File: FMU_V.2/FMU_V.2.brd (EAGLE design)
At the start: 90.2 x 95.9 mm, 322 parts, among them J201 HEADER_1X4, J202 HEADER_1X4, J203 HEADER_1X4, J204 HEADER_1X4, J301 HEADER_1X4, J302 HEADER_1X4, J303 HEADER_1X4, J401 HEADER_1X4, J402 HEADER_1X4, J403 HEADER_1X4, J404 HEADER_1X4, J701 HEADER_1X4, J901 HEADER_1X4, J902 HEADER_1X4, M3_MOUNT1 MOUNT-HOLE3.1MM, M3_MOUNT2 MOUNT-HOLE3.1MM, M3_MOUNT3 MOUNT-HOLE3.1MM, M3_MOUNT4 MOUNT-HOLE3.1MM, U101 STM32F4X7VX, U102 FM25V01, U201 TXS0108TSSOP-20, U202 LT3469, U301 2908-05WB-MG, U302 NUF2042XV6, U303 ADUM5402, U304 MAX13487E, U305 MAX232ECWE, U401 ADUM5402, U402 MAX3051, U403 MAX3051, U502 ICM20608-G, U503 MPU-9250, U504 MPU-6000, U506 MS5611-01BA, U601 BQ24315, U602 BQ24315, U603 LD1117ASTR, U604 LD1117ASTR, U701 STM32F10XCXT6, U801 TXS0108TSSOP-20, U803 LD1117ASTR, U901 LM5005, U902 LM5005, X101 NX3225SA-24.000MHZ-STD-CSR-1, X701 NX3225SA-24.000MHZ-STD-CSR-1

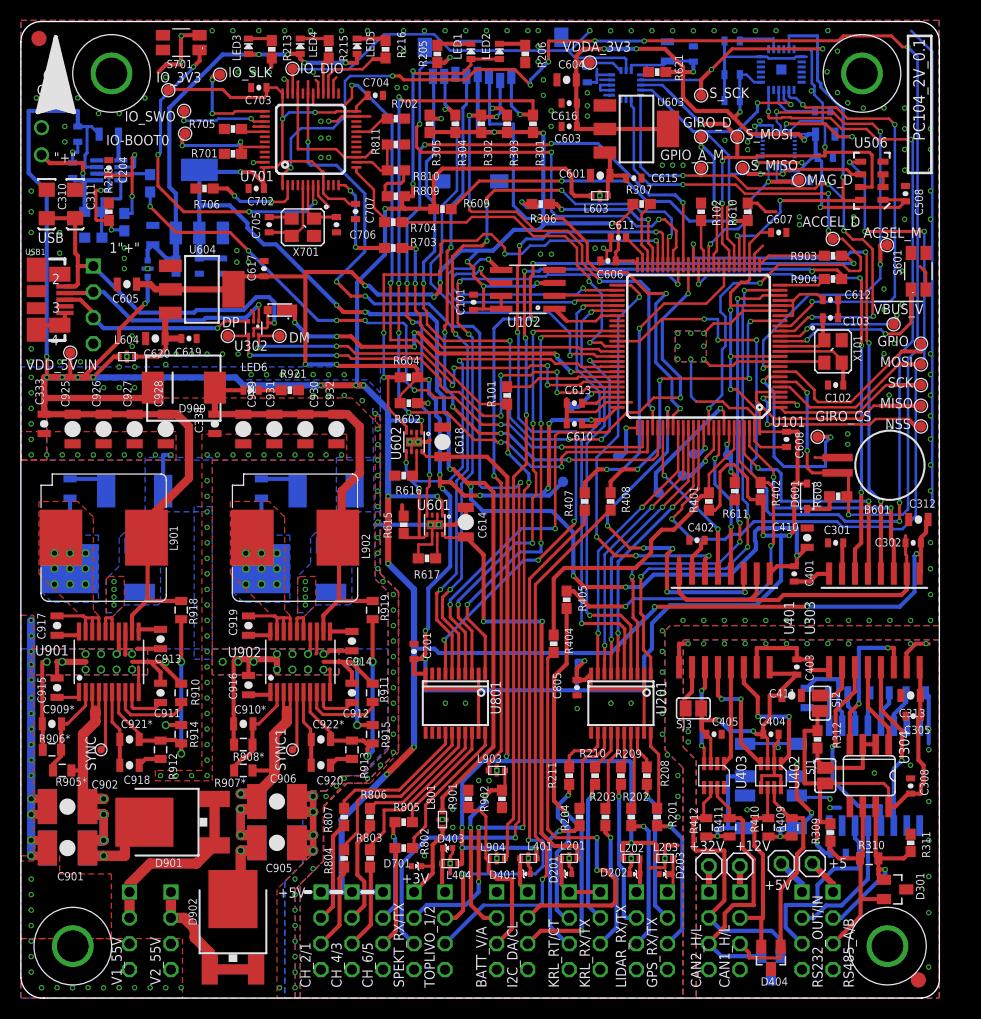
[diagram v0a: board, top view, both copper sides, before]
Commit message: Исправленно #2, #3, #5, #8, #9
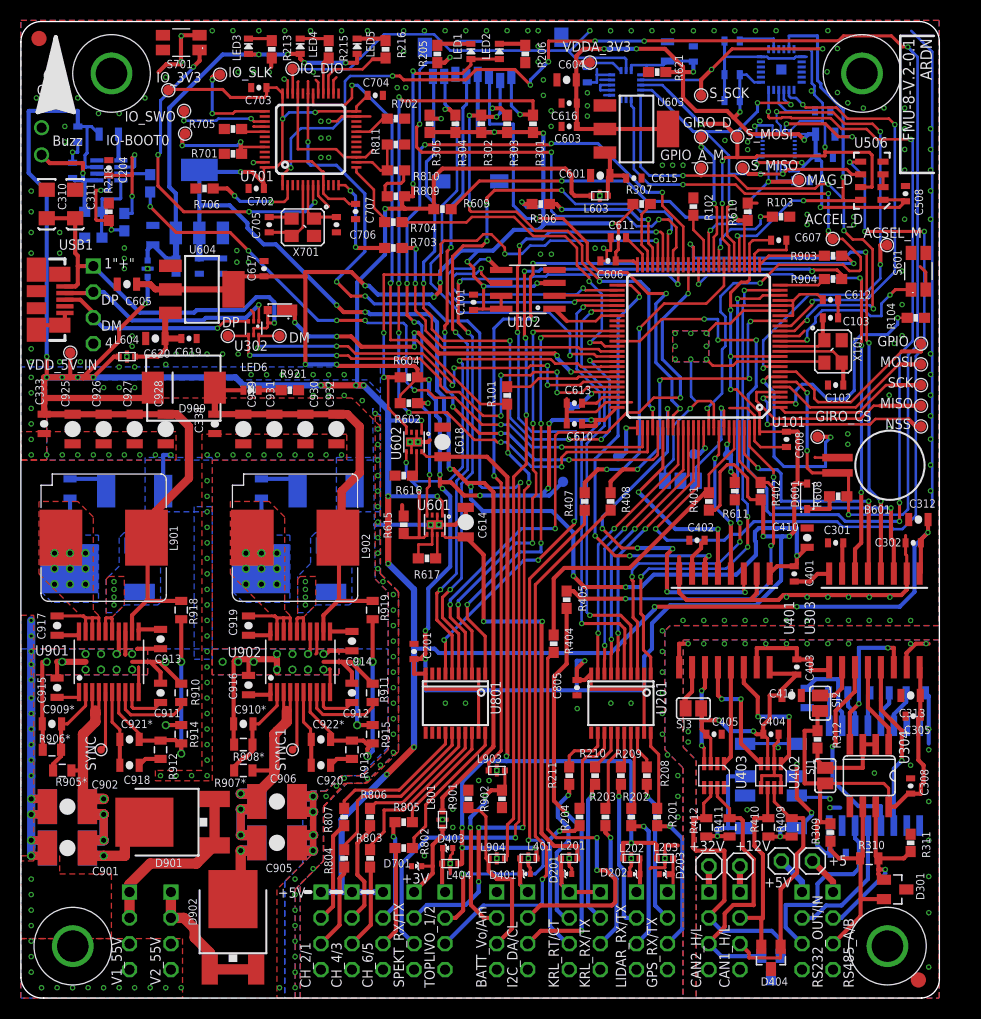
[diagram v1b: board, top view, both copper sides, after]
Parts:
- removed !VBUS_V, !VDD_BRICK, !VDD_SERVO: PAD.04, pixhawk2:PAD.04X.04
- added R103: 10K, pixhawk2:0603-RES
- added R104: 1M, pixhawk2:0603-RES
- added SJ4: (no value), jumper:SJ_2
- R706: value 10K -> 220R
- moved R102 0.92 mm to (66.0, 77.7)
- moved C607 0.76 mm to (74.4, 74.4)
- moved +5 0.25 mm to (77.7, 13.5)
- moved +5V 0.25 mm to (74.7, 13.5)
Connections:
- net PB2-BOOT1 renamed PC5
- removed net PRESSURE_SENS: U101.34
- removed net VDD_3V3_SENSORS_EN: U101.2
- new net N$14: R104.1, U101.2
- new net N$16: R103.1, U101.34
- net !VBUS_VALID: no longer !VBUS_V.P$1
- net !VDD_BRICK_VALID: now also SJ4.1; no longer !VDD_BRICK.P$1
- net !VDD_SERVO_VALID: now also SJ4.3; no longer !VDD_SERVO.P$1
- net GND: now also R103.2, R104.2, SJ4.2
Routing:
- net N$14: track 0.00 -> 21.2 mm, vias 0 -> 2
- net !VBUS_VALID: track 13.5 -> 2.63 mm, vias 2 -> 0
- net N$16: track 0.00 -> 8.99 mm, vias 0 -> 2
- net !VDD_BRICK_VALID: track 6.42 -> 13.2 mm
- net CAN1_RX: track 16.6 -> 21.0 mm
- net GND: track 447.0 -> 443.9 mm
- net !VDD_SERVO_VALID: track 13.2 -> 10.2 mm
- net !BARO_CS: track 79.0 -> 81.9 mm
- net VDD_5V_IN: track 356.1 -> 358.9 mm, vias 21 -> 22
- net VDD_3V3_SENSORS_EN: track 1.82 -> 0.00 mm, vias 1 -> 0
- net !MPU_CS: track 41.7 -> 40.3 mm
- net FMU-I2C1_SCL: track 32.8 -> 31.7 mm
- net N$19: track 3.28 -> 4.30 mm
- net MAG_DRDY: track 16.2 -> 17.2 mm
- net CAN1_TX: track 37.2 -> 38.1 mm
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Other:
- board text added: "BATT_Vo/Am"
- board text added: "Buzz"
- board text added: "DM"
- board text added: "DP"
- board text added: "FMU-8-V.2-0.1 ARDN"
- board text added: "QR"
- board text removed: ""+""
- board text removed: "2"
- board text removed: "3"
- board text removed: "BATT_V/A"
- board text removed: "PC104_2V_0.1"
- board text removed: "USB"
